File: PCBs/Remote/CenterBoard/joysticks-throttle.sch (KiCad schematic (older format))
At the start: 5 parts, among them U601 Joystick Left, U602 Joystick Right

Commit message: Centerboard v0.1 is done.
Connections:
- net GND: now also U601.S1 (SHIELD), U601.S2 (SHIELD), U601.S3 (SHIELD), U601.S4 (SHIELD), U602.S1 (SHIELD), U602.S2 (SHIELD), U602.S3 (SHIELD), U602.S4 (SHIELD)
- no-connect marks 2 -> 0
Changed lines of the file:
@@
 Text Label 8800 1850 2    50   ~ 0
 JS_left_H
-NoConn ~ 8900 2550
-NoConn ~ 8900 4300
 $Comp
 L power:+3V3 #PWR0116
@@
 Text GLabel 1500 1800 0    50   Input ~ 0
 Throttle
+$Comp
+L power:GND #PWR0107
+U 1 1 5FD8130D
+P 8900 4300
+F 0 "#PWR0107" H 8900 4050 50  0001 C CNN
+F 1 "GND" H 8905 4172 50  0000 R CNN
+F 2 "" H 8900 4300 50  0001 C CNN
+F 3 "" H 8900 4300 50  0001 C CNN
+	1    8900 4300
+	1    0    0    -1
+$EndComp
+$Comp
+L power:GND #PWR0108
+U 1 1 5FD819A5
+P 8900 2550
+F 0 "#PWR0108" H 8900 2300 50  0001 C CNN
+F 1 "GND" H 8905 2422 50  0000 R CNN
+F 2 "" H 8900 2550 50  0001 C CNN
+F 3 "" H 8900 2550 50  0001 C CNN
+	1    8900 2550
+	1    0    0    -1
+$EndComp
 $EndSCHEMATC

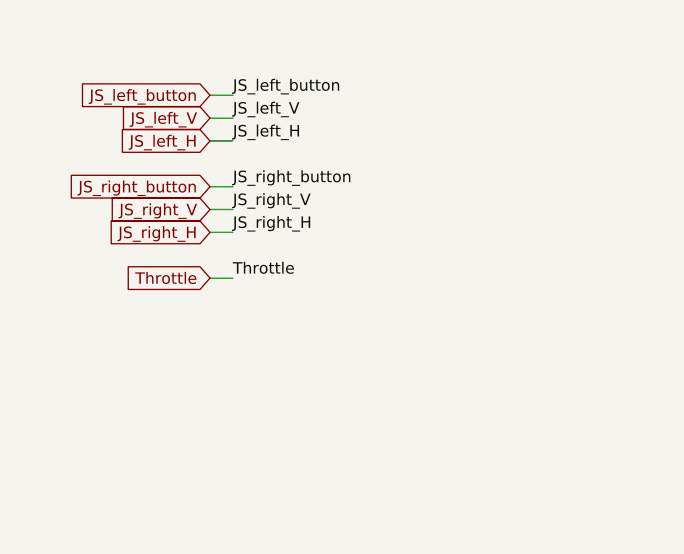
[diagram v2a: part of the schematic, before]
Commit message: More finishing work on remote-centerboard. Copied in the Drone main board, did some cleaning up on that. Started work on  more neat and clean lessons learned documents
Signed-off-by: Eldalote.Electronics <Eldalote.Electronics@gmail.com>
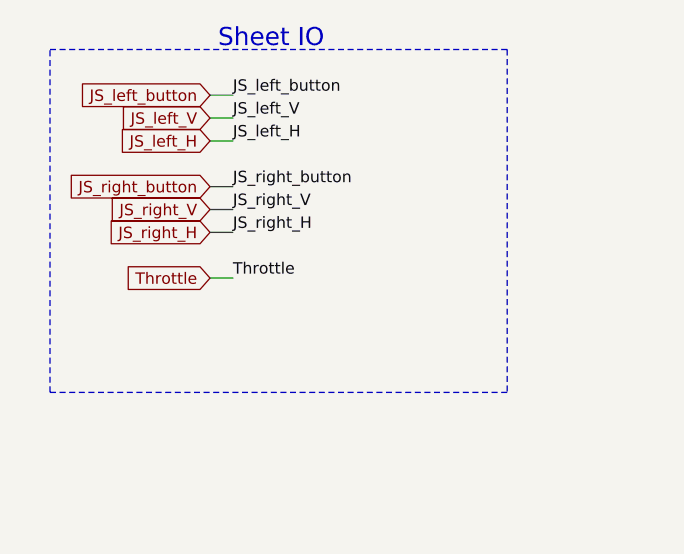
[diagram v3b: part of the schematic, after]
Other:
- note added: "Sheet IO"
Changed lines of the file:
@@
 	1    0    0    -1
 $EndComp
+Wire Notes Line
+	800  800  2800 800
+Wire Notes Line
+	2800 800  2800 2300
+Wire Notes Line
+	2800 2300 800  2300
+Wire Notes Line
+	800  2300 800  800
+Text Notes 2000 800  2    79   ~ 0
+Sheet IO
 $EndSCHEMATC

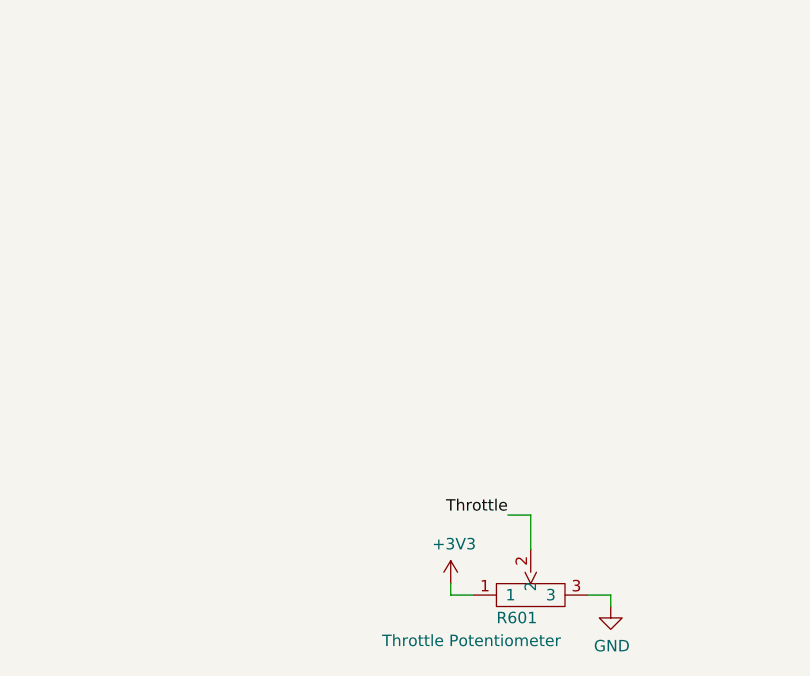
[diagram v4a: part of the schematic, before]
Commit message: Some cleanup, and PCB antenna removal.
Last edits before asking for reddit feedback.

Signed-off-by: Eldalote.Electronics <Eldalote.Electronics@gmail.com>
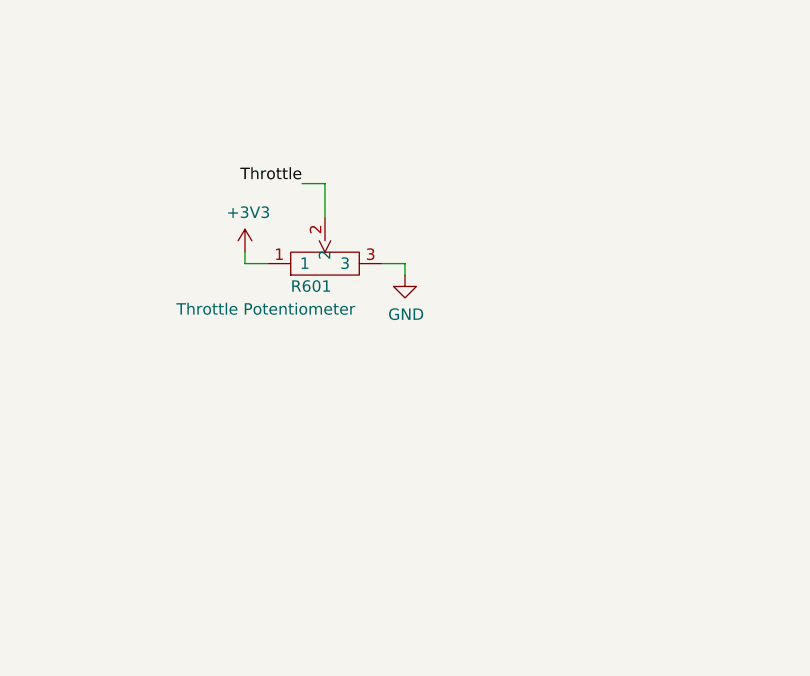
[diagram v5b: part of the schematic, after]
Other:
- moved on the sheet: R601
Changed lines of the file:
@@
 L Eldalote-General:PTA6043 R?
 U 1 1 5FB902BA
-P 5850 5150
+P 4950 3700
 AR Path="/5FB902BA" Ref="R?"  Part="1"
 AR Path="/5FB8F5C2/5FB902BA" Ref="R601"  Part="1"
-F 0 "R601" V 5750 5050 50  0000 R CNN
-F 1 "Throttle Potentiometer" V 5650 5550 50  0000 R CNN
-F 2 "Eldalote-footprints:PTA6043" H 5850 5150 50  0001 C CNN
-F 3 "" H 5850 5150 50  0001 C CNN
-F 4 "PTA6043-2015DPB103-ND " H 5850 5150 50  0001 C CNN "DigiKey"
-F 5 "652-PTA60432015DPB10 " H 5850 5150 50  0001 C CNN "Mouser"
-	1    5850 5150
+F 0 "R601" V 4850 3600 50  0000 R CNN
+F 1 "Throttle Potentiometer" V 4750 4100 50  0000 R CNN
+F 2 "Eldalote-footprints:PTA6043" H 4950 3700 50  0001 C CNN
+F 3 "" H 4950 3700 50  0001 C CNN
+F 4 "PTA6043-2015DPB103-ND " H 4950 3700 50  0001 C CNN "DigiKey"
+F 5 "652-PTA60432015DPB10 " H 4950 3700 50  0001 C CNN "Mouser"
+	1    4950 3700
 	0    -1   -1   0
 $EndComp
@@
 L power:+3V3 #PWR0128
 U 1 1 5FB9DFEF
-P 5750 5100
-F 0 "#PWR0128" H 5750 4950 50  0001 C CNN
-F 1 "+3V3" H 5765 5273 50  0000 C CNN
-F 2 "" H 5750 5100 50  0001 C CNN
-F 3 "" H 5750 5100 50  0001 C CNN
-	1    5750 5100
+P 4850 3650
+F 0 "#PWR0128" H 4850 3500 50  0001 C CNN
+F 1 "+3V3" H 4865 3823 50  0000 C CNN
+F 2 "" H 4850 3650 50  0001 C CNN
+F 3 "" H 4850 3650 50  0001 C CNN
+	1    4850 3650
 	1    0    0    -1
 $EndComp
@@
 L power:GND #PWR0129
 U 1 1 5FB9E77D
-P 6450 5200
-F 0 "#PWR0129" H 6450 4950 50  0001 C CNN
-F 1 "GND" H 6455 5027 50  0000 C CNN
-F 2 "" H 6450 5200 50  0001 C CNN
-F 3 "" H 6450 5200 50  0001 C CNN
-	1    6450 5200
-	1    0    0    -1
-$EndComp
-Wire Wire Line
-	6350 5150 6450 5150
-Wire Wire Line
-	6450 5150 6450 5200
-Wire Wire Line
-	5850 5150 5750 5150
-Wire Wire Line
-	5750 5150 5750 5100
-Wire Wire Line
-	6100 4950 6100 4800
-Wire Wire Line
-	6100 4800 6000 4800
-Text Label 6000 4800 2    50   ~ 0
+P 5550 3750
+F 0 "#PWR0129" H 5550 3500 50  0001 C CNN
+F 1 "GND" H 5555 3577 50  0000 C CNN
+F 2 "" H 5550 3750 50  0001 C CNN
+F 3 "" H 5550 3750 50  0001 C CNN
+	1    5550 3750
+	1    0    0    -1
+$EndComp
+Wire Wire Line
+	5450 3700 5550 3700
+Wire Wire Line
+	5550 3700 5550 3750
+Wire Wire Line
+	4950 3700 4850 3700
+Wire Wire Line
+	4850 3700 4850 3650
+Wire Wire Line
+	5200 3500 5200 3350
+Wire Wire Line
+	5200 3350 5100 3350
+Text Label 5100 3350 2    50   ~ 0
 Throttle
 Wire Wire Line
